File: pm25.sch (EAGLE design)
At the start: 36 parts, among them J1 CON-0024, Q1 TRANSISTOR-NPN-40V-0.2A-SOT23, Q2 TR-0001, U1 POWER-VREG-FB-EN-SW-350MA, U2 CCS811B-JOPD500, U3 POWER-SWITCH-SIP32509DT, U4 SI7021-A20-GM1R

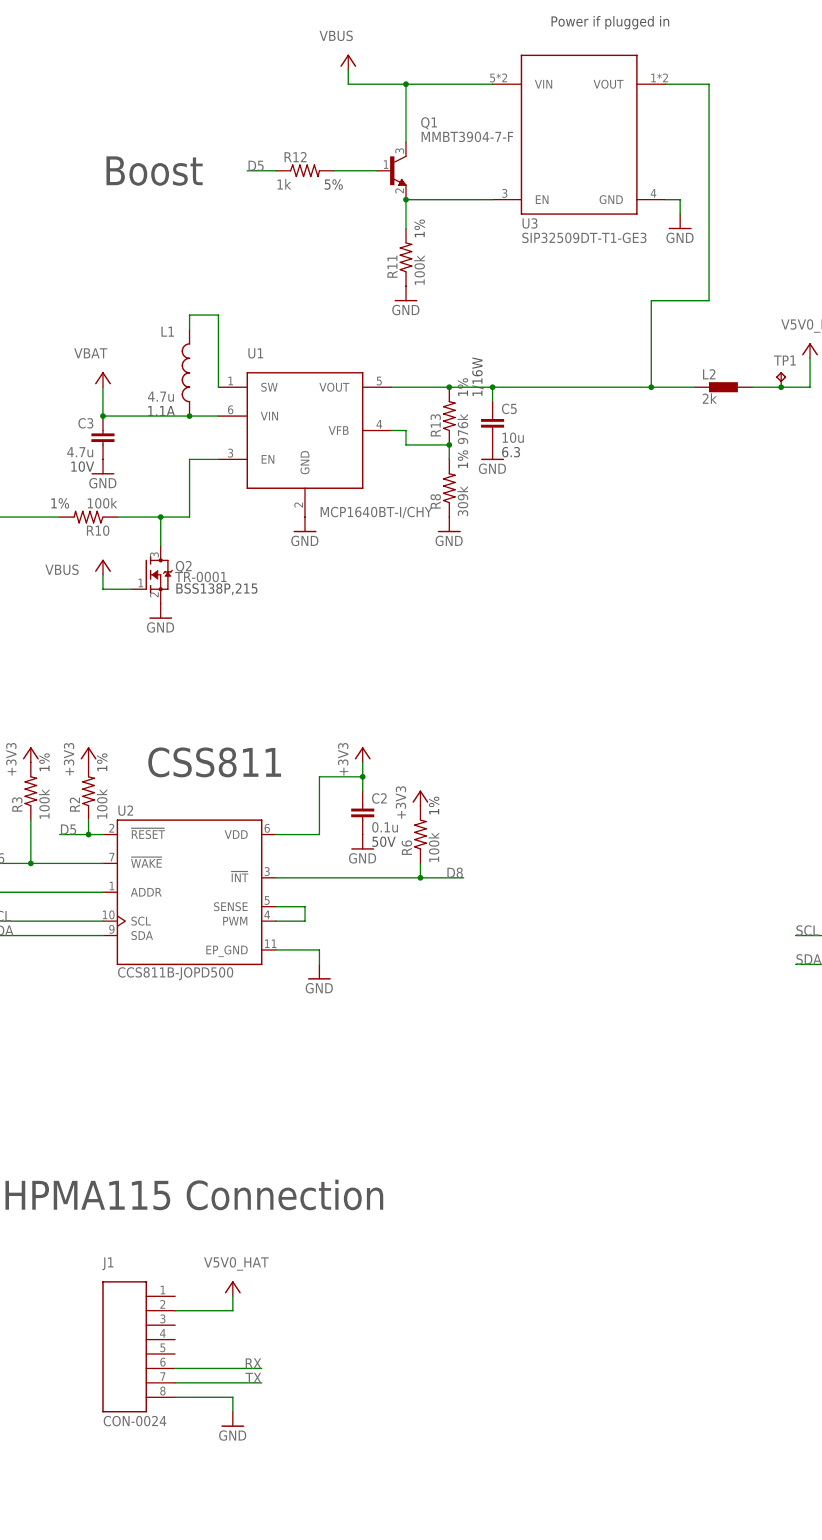
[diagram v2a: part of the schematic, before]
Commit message: Fixing issue with intermittent BOOST/USB control.
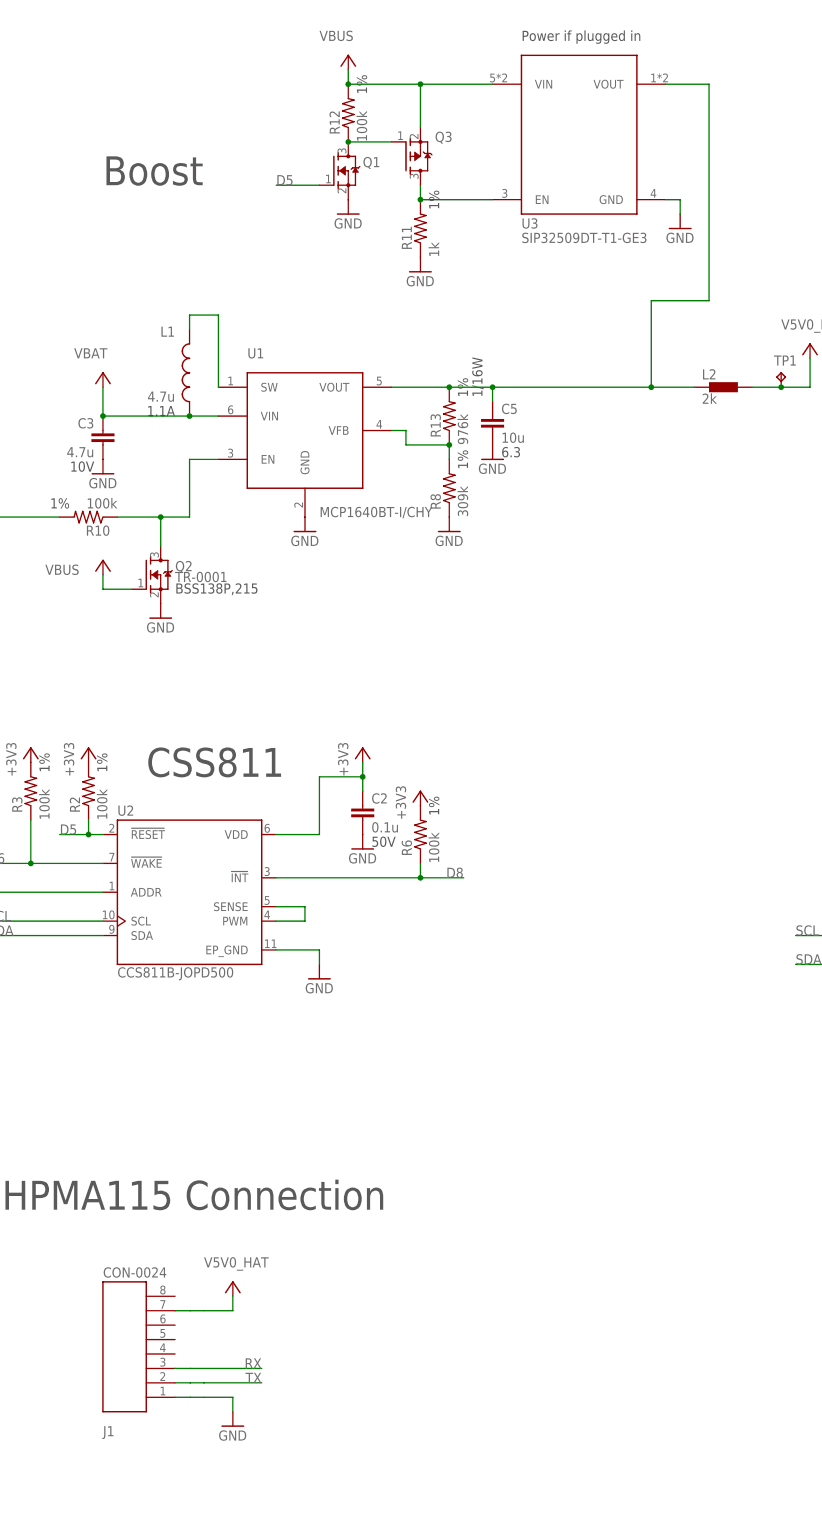
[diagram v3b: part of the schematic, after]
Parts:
- added Q3: TR-0003, wolff-den:TR-0003
- Q1: value TRANSISTOR-NPN-40V-0.2A-SOT23 -> TR-0001; device wolff-den:TRANSISTOR-NPN-40V-0.2A-SOT23 -> wolff-den:TR-0001
- R11: value 100k -> 1k; device wolff-den:RES-0041 -> wolff-den:RES-1K-1%-0402
- R12: value 1k -> 100k; device wolff-den:RES-0039 -> wolff-den:RES-0041
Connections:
- net D5: now also Q1.G; no longer R12.1
- net GND: now also J1.P$1, Q1.S; no longer J1.P$8
- net N$3: now also Q1.D, Q3.G, R12.1; no longer Q1.E, R11.2, U3.EN
- net N$7: now also Q3.D, R11.2, U3.EN; no longer Q1.B, R12.2
- net RX: now also J1.P$3; no longer J1.P$6
- net TX: now also J1.P$2; no longer J1.P$7
- net V5V0_HAT: now also J1.P$7; no longer J1.P$2
- net VBUS: now also Q3.S, R12.2; no longer Q1.C
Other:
- moved on the sheet: J1, R12

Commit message: Updating board based on recommendations
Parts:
- C2: value 0.1u -> 4.7u; device wolff-den:CAP-0017 -> wolff-den:CAP-0010
- R2, R3, R6, R9: value 100k -> 4.7k; device wolff-den:RES-0041 -> wolff-den:RES-4.7K-1%-0402

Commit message: Fixing load switch option
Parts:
- U3: value POWER-SWITCH-SIP32509DT -> POWER-SWITCH-SIP32508-SO23-6; device wolff-den:POWER-SWITCH-SIP32509DT -> wolff-den:POWER-SWITCH-SIP32508-SO23-6
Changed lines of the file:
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@@
 <part name="+3V2" library="supply1" library_urn="urn:adsk.eagle:library:371" deviceset="+3V3" device=""/>
 <part name="GND1" library="supply1" library_urn="urn:adsk.eagle:library:371" deviceset="GND" device=""/>
-<part name="U1" library="wolff-den" library_urn="urn:adsk.eagle:library:6370453" deviceset="POWER-VREG-FB-EN-SW" device="" package3d_urn="urn:adsk.eagle:package:5807329/2" technology="-350MA" value="POWER-VREG-FB-EN-SW-350MA"/>
+<part name="U1" library="wolff-den" library_urn="urn:adsk.eagle:library:6370453" deviceset="POWER-VREG-FB-EN-SW" device="" package3d_urn="urn:adsk.eagle:package:5807329/3" technology="-350MA" value="POWER-VREG-FB-EN-SW-350MA"/>
 <part name="GND2" library="supply1" library_urn="urn:adsk.eagle:library:371" deviceset="GND" device=""/>
 <part name="P+3" library="wolff-den" library_urn="urn:adsk.eagle:library:6370453" deviceset="VBUS" device=""/>
@@
 <part name="P+1" library="wolff-den" library_urn="urn:adsk.eagle:library:6370453" deviceset="VBUS" device=""/>
 <part name="GND13" library="supply1" library_urn="urn:adsk.eagle:library:371" deviceset="GND" device=""/>
-<part name="U3" library="wolff-den" library_urn="urn:adsk.eagle:library:6370453" deviceset="POWER-SWITCH" device="-SIP32509DT" package3d_urn="urn:adsk.eagle:package:5807329/2"/>
+<part name="U3" library="wolff-den" library_urn="urn:adsk.eagle:library:6370453" deviceset="POWER-SWITCH" device="-SO23-6" package3d_urn="urn:adsk.eagle:package:5807329/3" technology="-SIP32508"/>
 <part name="R11" library="wolff-den" library_urn="urn:adsk.eagle:library:6370453" deviceset="RES" device="-0402" package3d_urn="urn:adsk.eagle:package:5807335/4" technology="-1K-1%" value="1k"/>
 <part name="GND17" library="supply1" library_urn="urn:adsk.eagle:library:371" deviceset="GND" device=""/>
